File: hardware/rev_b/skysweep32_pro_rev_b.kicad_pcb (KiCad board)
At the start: 4 copper layers, 120 x 80 mm, 128 parts, among them J1 USB4105-GF-A, J10 1S VBAT SENSE ONLY, J11 310-101 VIBRATION MOTOR, J2 Ebyte E01-ML01DP5, J3 Ebyte E07-900M10S 855-925MHz, J4 Adafruit PID 3072 RFM95W, J5 Qualified 2012-layout RX5808, J6 Adafruit PID 746 Ultimate GPS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, J7 Adafruit PID 254 microSD, J8 OLED PHR-4 harness, J9 OPTIONAL I2C EXPANSION, Q1 AO3400A, Q2 AO3400A, SW1 RESET, SW2 BOOT, SW3 USER, U1 ESP32-S3-WROOM-1-N8, U2 LM73100RPWR, U3 AP63203WU-7, U4 USBLC6-2SC6

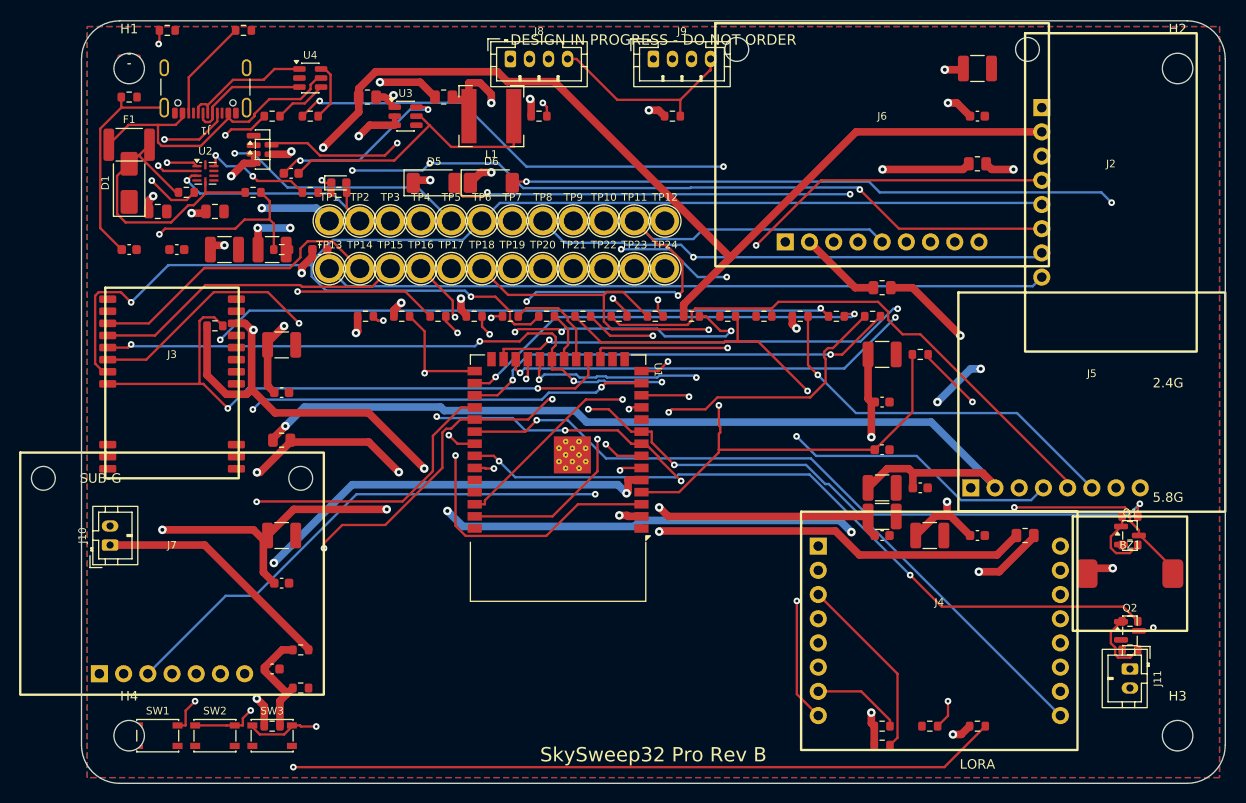
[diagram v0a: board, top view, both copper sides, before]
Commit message: feat(hardware): add 3D CAD enclosure previews and clean up silkscreen designators
- Render 3D Sentinel Enclosure Rev B previews (preview_enclosure_iso.png and preview_enclosure_interior.png) via FreeCAD and Matplotlib
- Clean component reference silkscreen designators (hide 0603/0805 passives ref text, format IC/module text) to prevent silk-over-copper overlaps
- Re-render PCB 3D previews with verified 3D STEP models
- Export combined Sentinel CAD assembly STEP skysweep32_pro_sentinel_assembly.step
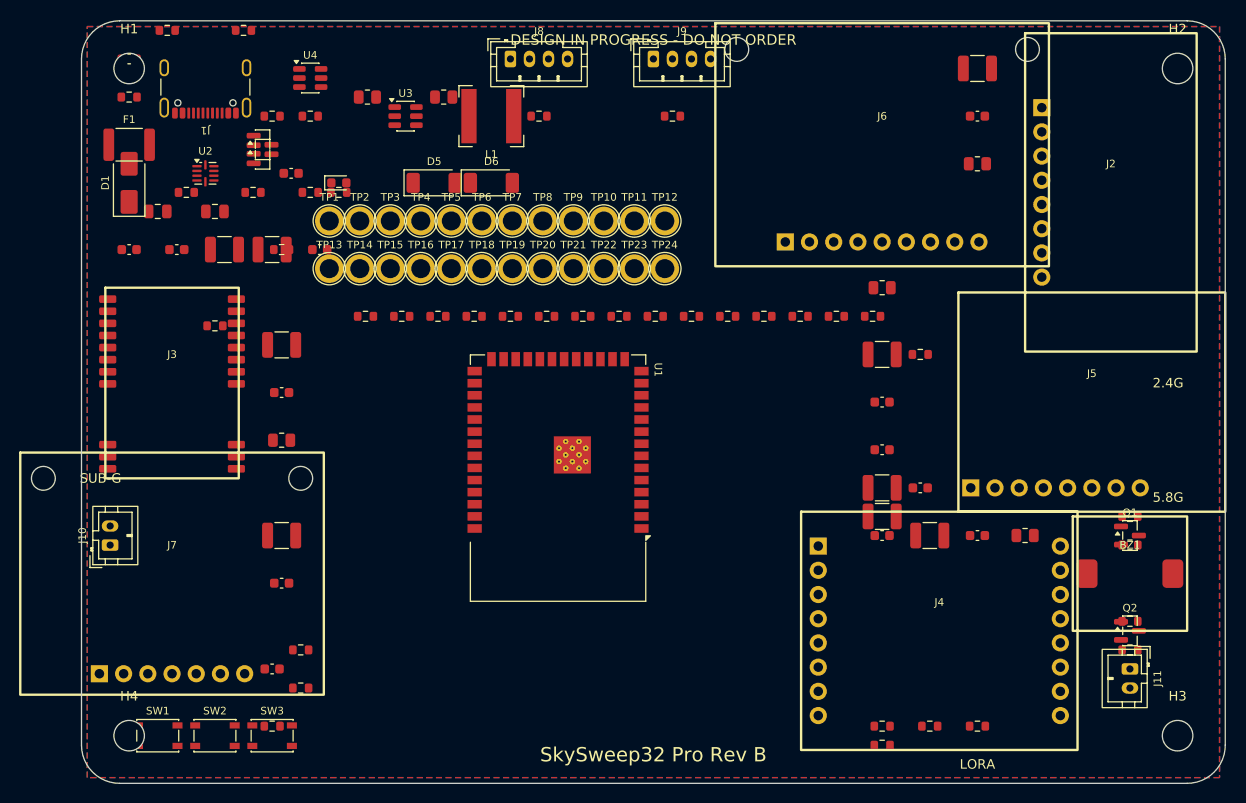
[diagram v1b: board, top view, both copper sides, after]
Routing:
- net RF_SPI_MOSI: track 234.1 -> 0.00 mm, vias 5 -> 0
- net RF_SPI_SCK: track 224.7 -> 0.00 mm, vias 2 -> 0
- net ESP_EN: track 197.3 -> 0.00 mm, vias 4 -> 0
- net RF_SPI_MISO: track 170.0 -> 0.00 mm, vias 5 -> 0
- net SD_CSN: track 160.9 -> 0.00 mm, vias 3 -> 0
- net VBUS_PROTECTED: track 150.9 -> 0.00 mm, vias 12 -> 0
- net VBAT_ADC: track 146.4 -> 0.00 mm, vias 4 -> 0
- net 3V3_CC: track 137.4 -> 0.00 mm, vias 4 -> 0
- net VBAT_SENSE_IN: track 134.5 -> 0.00 mm
- net 3V3_NRF: track 130.6 -> 0.00 mm, vias 2 -> 0
- net NRF24_CE: track 121.8 -> 0.00 mm, vias 2 -> 0
- net VIBRATION_DRAIN: track 119.8 -> 0.00 mm, vias 3 -> 0
- net 5V_SD: track 116.1 -> 0.00 mm, vias 3 -> 0
- net RX5808_RSSI: track 111.5 -> 0.00 mm, vias 4 -> 0
- net BUZZER_DRAIN: track 106.1 -> 0.00 mm, vias 3 -> 0
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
